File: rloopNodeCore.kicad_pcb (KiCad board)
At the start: 2 copper layers, 170 x 110 mm, 53 parts, among them P1 PWR_CONN_1X2, P2 PWR_CONN_1X2, P3 CAN_IN_M12, P4 CAN_OUT_M12, U1 R-625.0P, U2 MCP2562, U3 ISO1540, U4 TYS01

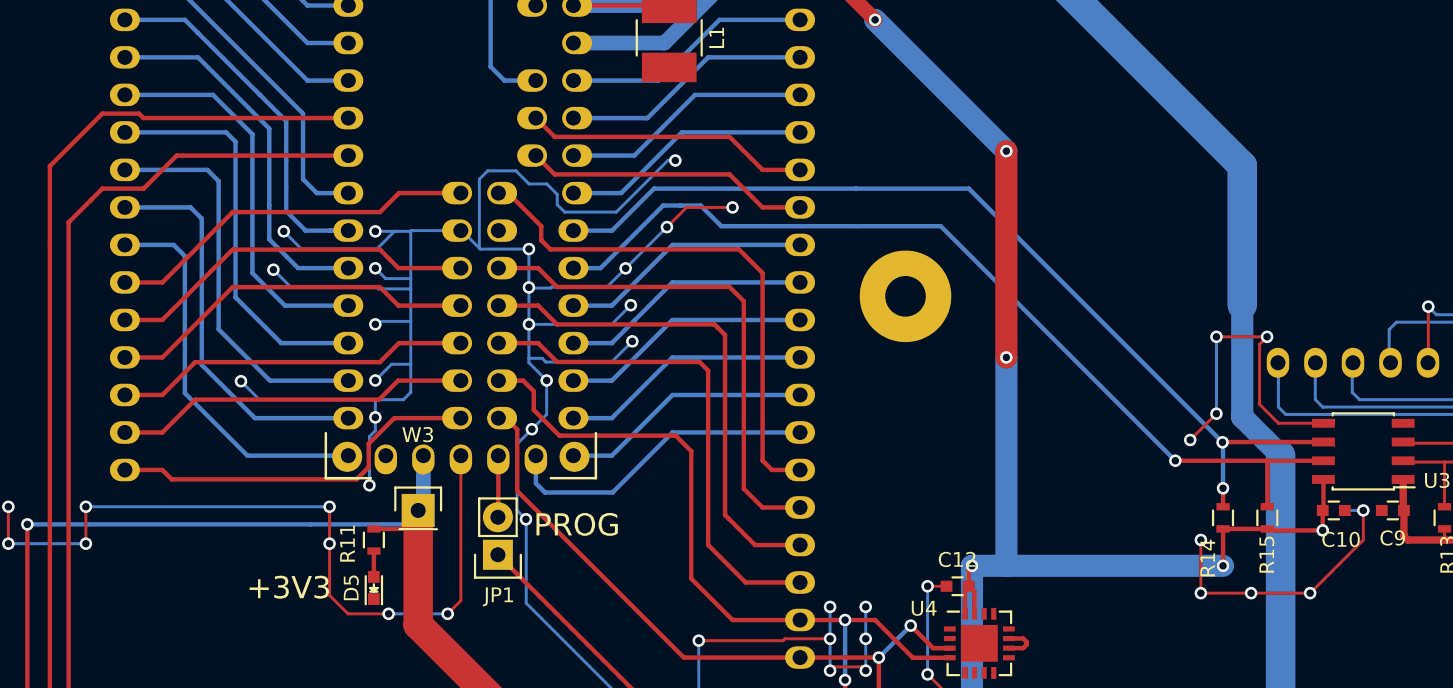
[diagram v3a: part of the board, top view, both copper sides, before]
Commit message: recovered lost ground traces
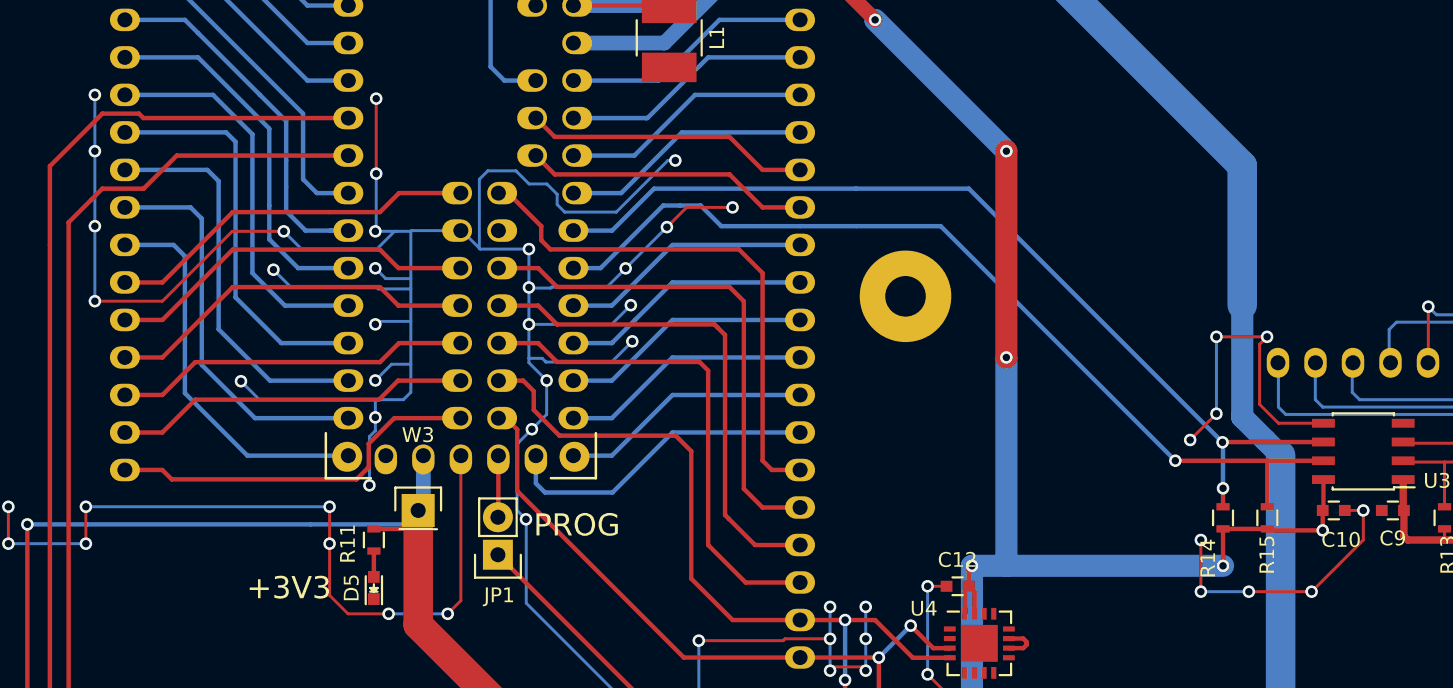
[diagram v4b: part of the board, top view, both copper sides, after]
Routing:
- net GND: track 291.1 -> 348.1 mm, vias 50 -> 61
- net (no net): track 19.3 -> 0.00 mm, vias 5 -> 0
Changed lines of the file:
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@@
     (thickness 1.6)
     (drawings 13)
-    (tracks 872)
+    (tracks 887)
     (zones 0)
     (modules 53)
@@
   )
   (gr_line (start 137.68 76.29) (end 137.68 90.26) (angle 90) (layer Cmts.User) (width 0.2))
-  (segment (start 208 98.6) (end 208 95) (width 0.2) (layer F.Cu) (net 0))
-  (segment (start 215.4 98.6) (end 211.4 98.6) (width 0.2) (layer F.Cu) (net 0))
-  (segment (start 219 93) (end 219 95) (width 0.2) (layer F.Cu) (net 0))
-  (segment (start 219 95) (end 215.4 98.6) (width 0.2) (layer F.Cu) (net 0))
-  (via (at 215.4 98.6) (size 0.85) (drill 0.5) (layers F.Cu B.Cu) (net 0))
-  (via (at 211.4 98.6) (size 0.85) (drill 0.5) (layers F.Cu B.Cu) (net 0))
-  (segment (start 211.4 98.6) (end 208 98.6) (width 0.2) (layer F.Cu) (net 0))
-  (via (at 208 98.6) (size 0.85) (drill 0.5) (layers F.Cu B.Cu) (net 0))
-  (via (at 208 95) (size 0.85) (drill 0.5) (layers F.Cu B.Cu) (net 0))
-  (segment (start 217.8 93) (end 219 93) (width 0.2) (layer B.Cu) (net 0))
-  (via (at 219 93) (size 0.85) (drill 0.5) (layers F.Cu B.Cu) (net 0))
   (segment (start 150.27 58.81) (end 147.505 58.81) (width 0.3) (layer B.Cu) (net 1))
   (segment (start 147.505 58.81) (end 138.315 49.62) (width 0.3) (layer B.Cu) (net 1))
@@
   (segment (start 238.27 129.09) (end 238.27 131.67) (width 1) (layer F.Cu) (net 31))
   (segment (start 238.27 131.67) (end 238.27 131.63) (width 1) (layer F.Cu) (net 31))
+  (segment (start 152.158 65.114) (end 152.158 70.194) (width 0.2) (layer F.Cu) (net 32))
+  (via (at 152.158 70.194) (size 0.85) (drill 0.5) (layers F.Cu B.Cu) (net 32))
+  (via (at 152.1 74.1) (size 0.85) (drill 0.5) (layers F.Cu B.Cu) (net 32))
+  (segment (start 152.158 70.194) (end 152.158 74.1) (width 0.2) (layer B.Cu) (net 32))
+  (via (at 152.158 65.114) (size 0.85) (drill 0.5) (layers F.Cu B.Cu) (net 32))
+  (segment (start 133.108 64.86) (end 133.108 68.67) (width 0.2) (layer B.Cu) (net 32))
+  (via (at 133.108 68.67) (size 0.85) (drill 0.5) (layers F.Cu B.Cu) (net 32))
+  (segment (start 133.108 73.75) (end 133.108 78.83) (width 0.2) (layer B.Cu) (net 32))
+  (segment (start 142.41 74.1) (end 137.68 78.83) (width 0.2) (layer F.Cu) (net 32))
+  (segment (start 137.68 78.83) (end 133.108 78.83) (width 0.2) (layer F.Cu) (net 32))
+  (via (at 133.108 78.83) (size 0.85) (drill 0.5) (layers F.Cu B.Cu) (net 32))
+  (segment (start 153.4 74.1) (end 153.5 74.1) (width 0.2) (layer B.Cu) (net 32))
+  (segment (start 153.4 74.1) (end 152.2 75.3) (width 0.2) (layer B.Cu) (net 32))
+  (segment (start 152.2 75.3) (end 147.1 75.3) (width 0.2) (layer B.Cu) (net 32))
+  (segment (start 147.1 75.3) (end 145.9 74.1) (width 0.2) (layer B.Cu) (net 32))
+  (via (at 145.9 74.1) (size 0.85) (drill 0.5) (layers F.Cu B.Cu) (net 32))
+  (segment (start 145.9 74.1) (end 142.41 74.1) (width 0.2) (layer F.Cu) (net 32))
+  (via (at 133.108 73.75) (size 0.85) (drill 0.5) (layers F.Cu B.Cu) (net 32))
+  (segment (start 133.108 68.67) (end 133.108 73.75) (width 0.2) (layer B.Cu) (net 32))
+  (via (at 133.108 64.86) (size 0.85) (drill 0.5) (layers F.Cu B.Cu) (net 32))
+  (segment (start 215.5 98.5) (end 211.25 98.5) (width 0.2) (layer F.Cu) (net 32))
+  (segment (start 219 95) (end 215.5 98.5) (width 0.2) (layer F.Cu) (net 32))
+  (via (at 215.5 98.5) (size 0.85) (drill 0.5) (layers F.Cu B.Cu) (net 32))
+  (segment (start 217.75 93) (end 219 93) (width 0.2) (layer F.Cu) (net 32) (status 400000))
+  (via (at 219 93) (size 0.85) (drill 0.5) (layers F.Cu B.Cu) (net 32))
+  (segment (start 219 93) (end 219 95) (width 0.2) (layer F.Cu) (net 32))
+  (via (at 208 95) (size 0.85) (drill 0.5) (layers F.Cu B.Cu) (net 32))
+  (segment (start 208 98.5) (end 208 95) (width 0.2) (layer F.Cu) (net 32))
+  (via (at 208 98.5) (size 0.85) (drill 0.5) (layers F.Cu B.Cu) (net 32))
+  (segment (start 211.25 98.5) (end 208 98.5) (width 0.2) (layer B.Cu) (net 32))
+  (via (at 211.25 98.5) (size 0.85) (drill 0.5) (layers F.Cu B.Cu) (net 32))
   (segment (start 108.75 124.25) (end 108.75 126.75) (width 0.2) (layer B.Cu) (net 32))
   (via (at 104.75 124.25) (size 0.85) (drill 0.5) (layers F.Cu B.Cu) (net 32))
@@
   (segment (start 152.8 77.3) (end 152.1 76.6) (width 0.2) (layer B.Cu) (net 32))
   (via (at 152.1 76.6) (size 0.85) (drill 0.5) (layers F.Cu B.Cu) (net 32))
-  (segment (start 153.5 74.1) (end 152.1 74.1) (width 0.2) (layer B.Cu) (net 32))
-  (via (at 152.1 74.1) (size 0.85) (drill 0.5) (layers F.Cu B.Cu) (net 32))
+  (segment (start 153.5 74.1) (end 152.158 74.1) (width 0.2) (layer B.Cu) (net 32))
+  (segment (start 152.158 74.1) (end 152.1 74.1) (width 0.2) (layer B.Cu) (net 32))
   (segment (start 154.5 74.1) (end 153.5 74.1) (width 0.2) (layer B.Cu) (net 32))
-  (segment (start 153.5 74.1) (end 153.4 74.1) (width 0.2) (layer B.Cu) (net 32))
-  (segment (start 153.4 74.1) (end 152.2 75.3) (width 0.2) (layer B.Cu) (net 32))
-  (segment (start 152.2 75.3) (end 147.1 75.3) (width 0.2) (layer B.Cu) (net 32))
-  (segment (start 147.1 75.3) (end 145.9 74.1) (width 0.2) (layer B.Cu) (net 32))
-  (via (at 145.9 74.1) (size 0.85) (drill 0.5) (layers F.Cu B.Cu) (net 32))
   (segment (start 154.5 78) (end 152.3 78) (width 0.2) (layer B.Cu) (net 32))
   (segment (start 152.3 78) (end 152.2 77.9) (width 0.2) (layer B.Cu) (net 32))
